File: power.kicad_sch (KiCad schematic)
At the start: 19 parts, among them U13 ACS712xLCTR-20A, U14 ACS712xLCTR-5A

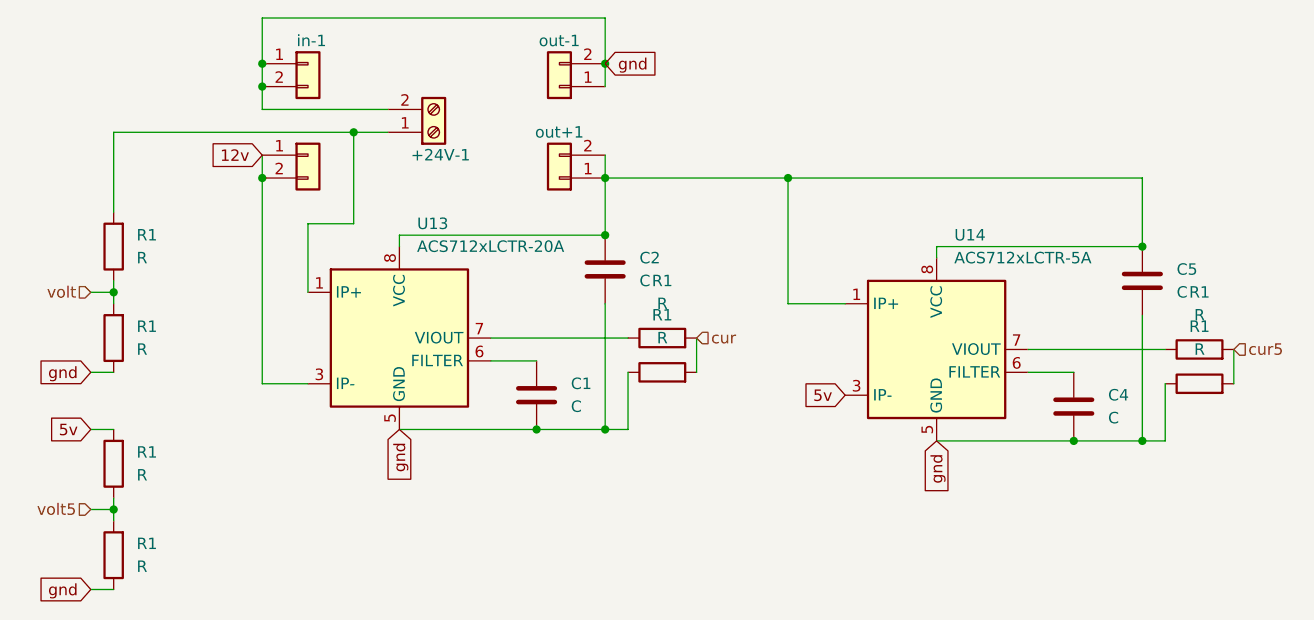
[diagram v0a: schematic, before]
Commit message: fixing labels / add some values
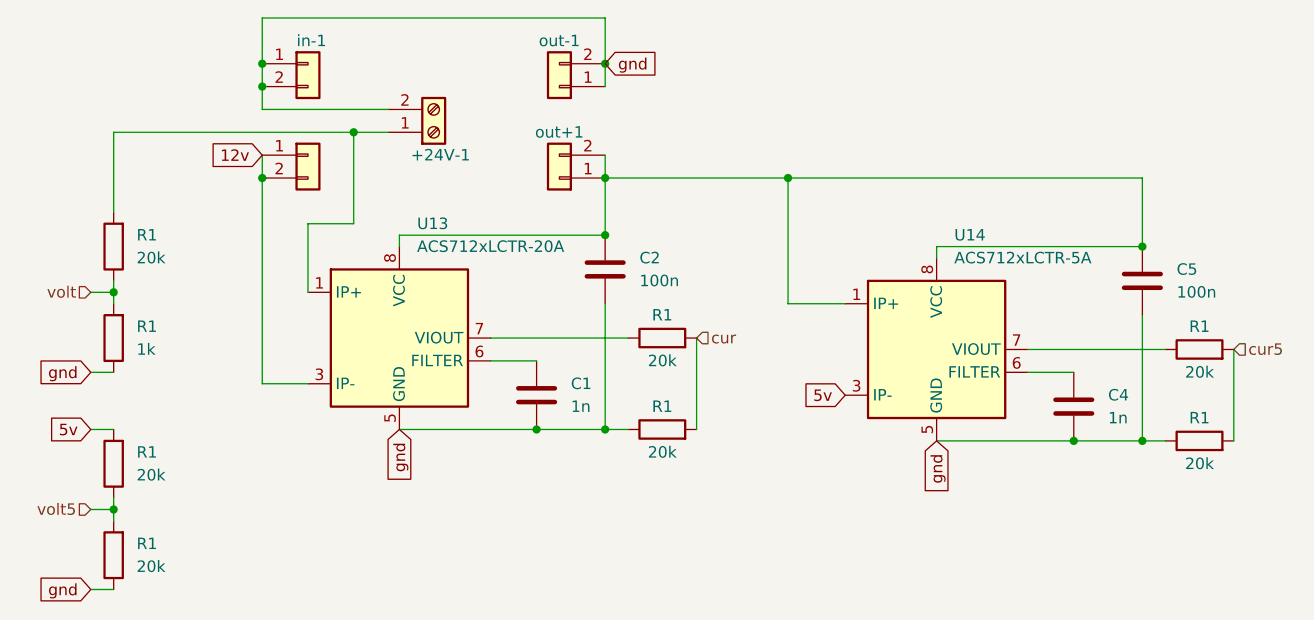
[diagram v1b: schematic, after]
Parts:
- C1, C4: value C -> 1n
- C2, C5: value C -> 100n
- R1: value R -> 20k
- R1: value R -> 1k
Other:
- moved on the sheet: R1
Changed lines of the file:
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@@
     (stroke (width 0) (type default))
   )
-  (wire (pts (xy 215.9 81.28) (xy 215.9 85.09))
+  (wire (pts (xy 215.9 81.28) (xy 215.9 91.44))
     (stroke (width 0) (type default))
   )
@@
     (stroke (width 0) (type default))
   )
-  (wire (pts (xy 156.21 80.01) (xy 156.21 83.82))
+  (wire (pts (xy 156.21 80.01) (xy 156.21 90.17))
     (stroke (width 0) (type default))
   )
@@
     (stroke (width 0) (type default))
   )
-  (wire (pts (xy 208.28 85.09) (xy 208.28 91.44))
-    (stroke (width 0) (type default))
-  )
   (wire (pts (xy 91.44 74.93) (xy 91.44 76.2))
     (stroke (width 0) (type default))
@@
   )
   (wire (pts (xy 91.44 97.79) (xy 91.44 99.06))
-    (stroke (width 0) (type default))
-  )
-  (wire (pts (xy 148.59 83.82) (xy 148.59 90.17))
     (stroke (width 0) (type default))
   )
@@
       (effects (font (size 1.27 1.27)) (justify left))
     )
-    (property "Value" "C" (at 149.86 73.66 0)
+    (property "Value" "100n" (at 149.86 73.66 0)
       (effects (font (size 1.27 1.27)) (justify left))
     )
@@
     )
   )
-  (symbol (lib_id "Device:R") (at 152.4 83.82 90) (unit 1)
-    (in_bom yes) (on_board yes) (dnp no) (fields_autoplaced)
-    (property "Reference" "R1" (at 152.4 77.47 90)
-      (effects (font (size 1.27 1.27)))
-    )
-    (property "Value" "R" (at 152.4 80.01 90)
-      (effects (font (size 1.27 1.27)))
-    )
-    (property "Footprint" "Resistor_SMD:R_1206_3216Metric" (at 152.4 85.598 90)
-      (effects (font (size 1.27 1.27)) hide)
-    )
-    (property "Datasheet" "~" (at 152.4 83.82 0)
+  (symbol (lib_id "Device:R") (at 152.4 90.17 90) (unit 1)
+    (in_bom yes) (on_board yes) (dnp no)
+    (property "Reference" "R1" (at 152.4 87.63 90)
+      (effects (font (size 1.27 1.27)))
+    )
+    (property "Value" "20k" (at 152.4 92.71 90)
+      (effects (font (size 1.27 1.27)))
+    )
+    (property "Footprint" "Resistor_SMD:R_1206_3216Metric" (at 152.4 91.948 90)
+      (effects (font (size 1.27 1.27)) hide)
+    )
+    (property "Datasheet" "~" (at 152.4 90.17 0)
       (effects (font (size 1.27 1.27)) hide)
     )
@@
       (effects (font (size 1.27 1.27)) (justify right))
     )
-    (property "Value" "R" (at 93.98 71.12 0)
+    (property "Value" "20k" (at 93.98 71.12 0)
       (effects (font (size 1.27 1.27)) (justify right))
     )
@@
       (effects (font (size 1.27 1.27)) (justify left))
     )
-    (property "Value" "C" (at 201.93 88.9 0)
+    (property "Value" "1n" (at 201.93 88.9 0)
       (effects (font (size 1.27 1.27)) (justify left))
     )
@@
   )
   (symbol (lib_id "Device:R") (at 152.4 80.01 90) (unit 1)
-    (in_bom yes) (on_board yes) (dnp no) (fields_autoplaced)
-    (property "Reference" "R1" (at 152.4 73.66 90)
-      (effects (font (size 1.27 1.27)))
-    )
-    (property "Value" "R" (at 152.4 76.2 90)
+    (in_bom yes) (on_board yes) (dnp no)
+    (property "Reference" "R1" (at 152.4 77.47 90)
+      (effects (font (size 1.27 1.27)))
+    )
+    (property "Value" "20k" (at 152.4 82.55 90)
       (effects (font (size 1.27 1.27)))
     )
@@
       (effects (font (size 1.27 1.27)) (justify right))
     )
-    (property "Value" "R" (at 93.98 95.25 0)
+    (property "Value" "20k" (at 93.98 95.25 0)
       (effects (font (size 1.27 1.27)) (justify right))
     )
@@
       (effects (font (size 1.27 1.27)) (justify left))
     )
-    (property "Value" "C" (at 142.24 87.63 0)
+    (property "Value" "1n" (at 142.24 87.63 0)
       (effects (font (size 1.27 1.27)) (justify left))
     )
@@
       (effects (font (size 1.27 1.27)) (justify right))
     )
-    (property "Value" "R" (at 93.98 81.28 0)
+    (property "Value" "1k" (at 93.98 81.28 0)
       (effects (font (size 1.27 1.27)) (justify right))
     )
@@
     )
   )
-  (symbol (lib_id "Device:R") (at 212.09 85.09 90) (unit 1)
-    (in_bom yes) (on_board yes) (dnp no) (fields_autoplaced)
-    (property "Reference" "R1" (at 212.09 78.74 90)
-      (effects (font (size 1.27 1.27)))
-    )
-    (property "Value" "R" (at 212.09 81.28 90)
-      (effects (font (size 1.27 1.27)))
-    )
-    (property "Footprint" "Resistor_SMD:R_1206_3216Metric" (at 212.09 86.868 90)
-      (effects (font (size 1.27 1.27)) hide)
-    )
-    (property "Datasheet" "~" (at 212.09 85.09 0)
+  (symbol (lib_id "Device:R") (at 212.09 91.44 90) (unit 1)
+    (in_bom yes) (on_board yes) (dnp no)
+    (property "Reference" "R1" (at 212.09 88.9 90)
+      (effects (font (size 1.27 1.27)))
+    )
+    (property "Value" "20k" (at 212.09 93.98 90)
+      (effects (font (size 1.27 1.27)))
+    )
+    (property "Footprint" "Resistor_SMD:R_1206_3216Metric" (at 212.09 93.218 90)
+      (effects (font (size 1.27 1.27)) hide)
+    )
+    (property "Datasheet" "~" (at 212.09 91.44 0)
       (effects (font (size 1.27 1.27)) hide)
     )
@@
   )
   (symbol (lib_id "Device:R") (at 212.09 81.28 90) (unit 1)
-    (in_bom yes) (on_board yes) (dnp no) (fields_autoplaced)
-    (property "Reference" "R1" (at 212.09 74.93 90)
-      (effects (font (size 1.27 1.27)))
-    )
-    (property "Value" "R" (at 212.09 77.47 90)
+    (in_bom yes) (on_board yes) (dnp no)
+    (property "Reference" "R1" (at 212.09 78.74 90)
+      (effects (font (size 1.27 1.27)))
+    )
+    (property "Value" "20k" (at 212.09 83.82 90)
       (effects (font (size 1.27 1.27)))
     )
@@
       (effects (font (size 1.27 1.27)) (justify left))
     )
-    (property "Value" "C" (at 209.55 74.93 0)
+    (property "Value" "100n" (at 209.55 74.93 0)
       (effects (font (size 1.27 1.27)) (justify left))
     )
@@
       (effects (font (size 1.27 1.27)) (justify right))
     )
-    (property "Value" "R" (at 93.98 105.41 0)
+    (property "Value" "20k" (at 93.98 105.41 0)
       (effects (font (size 1.27 1.27)) (justify right))
     )
